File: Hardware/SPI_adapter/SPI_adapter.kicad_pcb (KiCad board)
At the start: 4 copper layers, 99.5 x 34.5 mm, 5 parts, among them J1 Conn_02x07_Top_Bottom, J2 Conn_Coaxial, U1 RF-LORA-868-SO

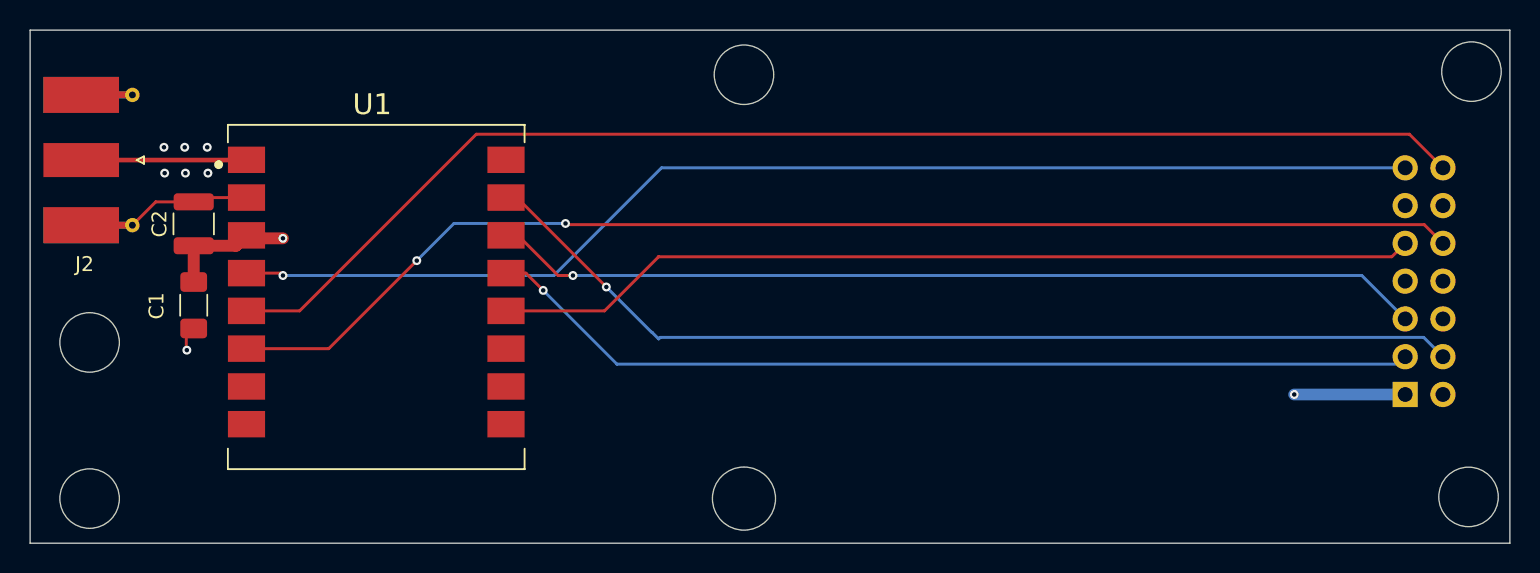
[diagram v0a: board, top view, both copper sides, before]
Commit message: Fixed USB traces, radio connectors, finished UART adapter
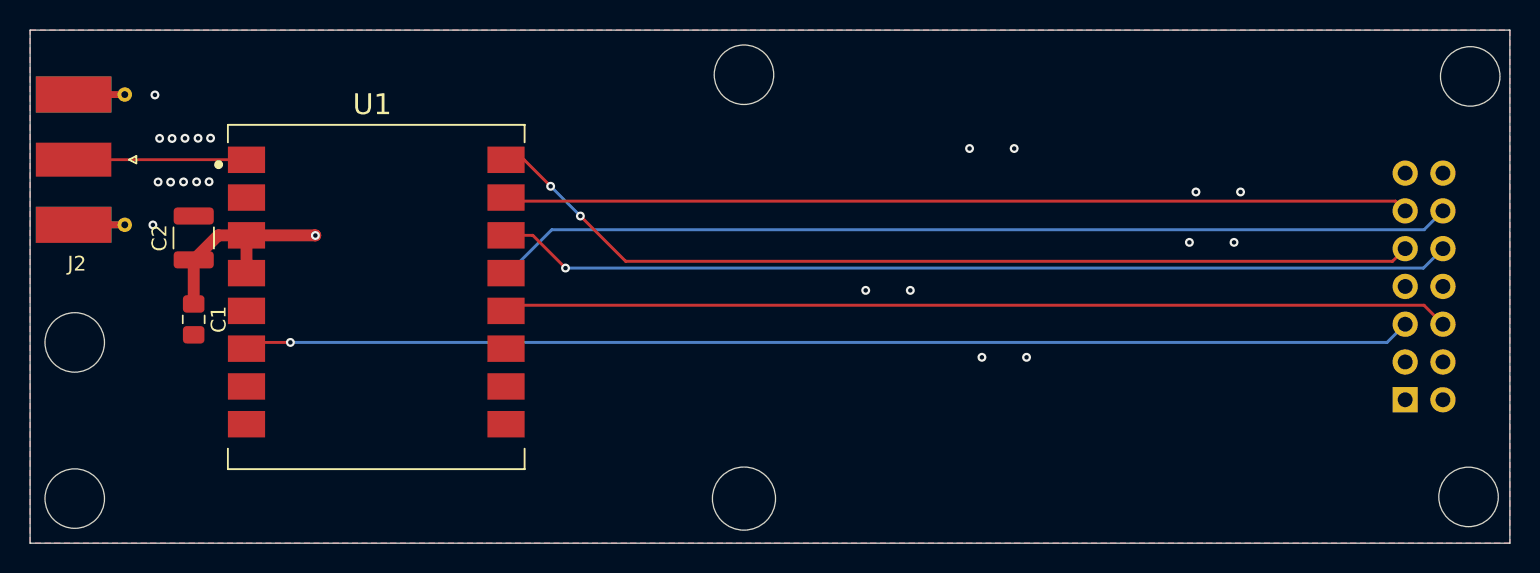
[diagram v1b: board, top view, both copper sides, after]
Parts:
- C1: footprint Capacitor_SMD:C_1206_3216Metric_Pad1.33x1.80mm_HandSolder -> Capacitor_SMD:C_0805_2012Metric_Pad1.18x1.45mm_HandSolder
- moved C1 0.95 mm to (88.5, 112.0)
- moved C2 0.95 mm to (88.5, 106.5)
- moved J2 0.51 mm to (82.1, 101.2)
- moved J1 0.36 mm to (170.0, 117.4)
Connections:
- J1 pad 1: +3.3V -> unconnected-(J1-Pin_1-Pad1)
- J1 pad 10: /RADIO_DIO1 -> /SPI_MISO
- J1 pad 11: /RADIO_BUSY -> /SPI_MOSI
- J1 pad 12: GND -> /SPI_SCK
- J1 pad 13: /GPIO1 -> GND
- J1 pad 14: /GPIO2 -> +3.3V
- J1 pad 2: GND -> unconnected-(J1-Pin_2-Pad2)
- J1 pad 3: /SPI_SCK -> GND
- J1 pad 4: /SPI_MOSI -> /RADIO_BUSY
- J1 pad 5: /SPI_MISO -> /RADIO_DIO1
- J1 pad 6: unconnected-(J1-Pin_6-Pad6) -> /RADIO_RST
- J1 pad 7: /RADIO_RX -> /RADIO_TX
- J1 pad 8: /RADIO_TX -> /RADIO_RX
- J1 pad 9: /RADIO_RST -> /SPI_CS
- U1 pad 4: /GPIO1 -> +3.3V
- U1 pad 5: /GPIO2 -> GND
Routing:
- net /GPIO2: track 86.3 -> 0.00 mm
- net /GPIO1: track 81.0 -> 0.00 mm, vias 1 -> 0
- net /SPI_CS: track 0.00 -> 63.6 mm, vias 0 -> 2
- net GND: track 11.3 -> 0.00 mm, vias 7 -> 22
- net /SPI_MOSI: track 67.5 -> 60.8 mm, vias 1 -> 0
- net +3.3V: track 88.6 -> 94.5 mm, vias 2 -> 1
- net /RADIO_DIO1: track 84.5 -> 78.6 mm, vias 2 -> 1
- net /SPI_MISO: track 62.8 -> 64.5 mm
- net /SPI_SCK: track 63.2 -> 64.8 mm, vias 1 -> 0
- net /RADIO_RST: track 62.4 -> 63.7 mm
- net /RF_ANT: track 11.1 -> 11.6 mm
- added copper zone on B.Cu, net GND
- added copper zone on F.Cu, net GND
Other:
- outline, holes or cut-outs redrawn
